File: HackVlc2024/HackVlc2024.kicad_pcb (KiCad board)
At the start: 2 copper layers, 75 x 80 mm, 10 parts, among them J1 Entrada Alimentación, J10 LDR, J2 ESP32_IZQ, J3 ESP32_DER, J4 Neopixel, J5 Lamas, J6 Bomba, J7 Suelo, J8 DH11, J9 Bomba

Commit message: Serigrafia
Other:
- board text added: "Bomba"
- board text added: "DH11"
- board text added: "Entrada Alimentación"
- board text added: "LDR"
- board text added: "Lamas"
- board text added: "Neopixel"
- board text added: "Nivel Tanque"
- board text added: "Suelo"
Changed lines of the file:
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@@
 		(tags "connector JST XH vertical")
 		(property "Reference" "J10"
-			(at 2.5 -3.55 180)
+			(at -6.524 3.344 180)
 			(layer "F.SilkS")
 			(effects
@@
 		(tags "connector JST XH vertical")
 		(property "Reference" "J6"
-			(at 2.5 -3.55 180)
+			(at -6.016 3.344 180)
 			(layer "F.SilkS")
 			(effects
@@
 		(tags "connector JST XH vertical")
 		(property "Reference" "J7"
-			(at 2.5 -3.55 180)
+			(at -6.016 3.344 180)
 			(layer "F.SilkS")
 			(effects
@@
 		(tags "connector JST XH vertical")
 		(property "Reference" "J9"
-			(at 3.75 -3.55 180)
+			(at -6.016 3.81 180)
 			(layer "F.SilkS")
 			(effects
@@
 		(tags "connector JST XH vertical")
 		(property "Reference" "J4"
-			(at 2.5 -3.55 180)
+			(at -6.016 3.344 180)
 			(layer "F.SilkS")
 			(effects
@@
 		(tags "connector JST XH vertical")
 		(property "Reference" "J5"
-			(at 2.5 -3.55 180)
+			(at -6.016 3.344 180)
 			(layer "F.SilkS")
 			(effects
@@
 		(tags "connector JST XH vertical")
 		(property "Reference" "J8"
-			(at 2.5 -3.55 180)
+			(at -6.016 3.344 180)
 			(layer "F.SilkS")
 			(effects
@@
 		(layer "Edge.Cuts")
 	)
+	(gr_text "Suelo"
+		(at 137.668 72.5035 0)
+		(layer "F.SilkS")
+		(effects
+			(font
+				(size 1.5 1.5)
+				(thickness 0.2)
+			)
+			(justify left bottom)
+		)
+	)
+	(gr_text "Bomba"
+		(at 137.668 64.3825 0)
+		(layer "F.SilkS")
+		(effects
+			(font
+				(size 1.5 1.5)
+				(thickness 0.2)
+			)
+			(justify left bottom)
+		)
+	)
+	(gr_text "Nivel\nTanque"
+		(at 137.668 98.073958 0)
+		(layer "F.SilkS")
+		(effects
+			(font
+				(size 1.5 1.5)
+				(thickness 0.2)
+			)
+			(justify left bottom)
+		)
+	)
+	(gr_text "Lamas"
+		(at 137.668 56.2615 0)
+		(layer "F.SilkS")
+		(effects
+			(font
+				(size 1.5 1.5)
+				(thickness 0.2)
+			)
+			(justify left bottom)
+		)
+	)
+	(gr_text "Neopixel"
+		(at 137.668 48.1405 0)
+		(layer "F.SilkS")
+		(effects
+			(font
+				(size 1.5 1.5)
+				(thickness 0.2)
+			)
+			(justify left bottom)
+		)
+	)
+	(gr_text "Entrada Alimentación"
+		(at 90.678 43.942 0)
+		(layer "F.SilkS")
+		(effects
+			(font
+				(size 1.5 1.5)
+				(thickness 0.2)
+				(bold yes)
+			)
+			(justify left bottom)
+		)
+	)
+	(gr_text "LDR"
+		(at 137.668 88.7455 0)
+		(layer "F.SilkS")
+		(effects
+			(font
+				(size 1.5 1.5)
+				(thickness 0.2)
+			)
+			(justify left bottom)
+		)
+	)
+	(gr_text "DH11"
+		(at 137.668 80.6245 0)
+		(layer "F.SilkS")
+		(effects
+			(font
+				(size 1.5 1.5)
+				(thickness 0.2)
+			)
+			(justify left bottom)
+		)
+	)
+	(segment
+		(start 130.81 42.418)
+		(end 132.668 44.276)
+		(width 1.5)
+		(layer "B.Cu")
+		(net 1)
+	)
 	(segment
 		(start 100.584 55.626)
@@
 	)
 	(segment
+		(start 115.824 46.228)
+		(end 119.634 42.418)
+		(width 1.5)
+		(layer "B.Cu")
+		(net 1)
+	)
+	(segment
 		(start 132.668 88.399)
 		(end 132.668 96.52)
@@
 	)
 	(segment
-		(start 115.824 46.228)
-		(end 120.142 41.91)
+		(start 119.634 42.418)
+		(end 130.81 42.418)
 		(width 1.5)
 		(layer "B.Cu")
@@
 	)
 	(segment
-		(start 120.142 41.91)
-		(end 130.302 41.91)
-		(width 1.5)
-		(layer "B.Cu")
-		(net 1)
-	)
-	(segment
 		(start 132.668 47.794)
 		(end 132.668 55.915)
@@
 	)
 	(segment
-		(start 132.668 64.036)
-		(end 132.668 72.157)
+		(start 115.824 55.626)
+		(end 115.824 46.228)
 		(width 1.5)
 		(layer "B.Cu")
@@
 	)
 	(segment
-		(start 115.824 55.626)
-		(end 115.824 46.228)
+		(start 132.668 64.036)
+		(end 132.668 72.157)
 		(width 1.5)
 		(layer "B.Cu")
@@
 	)
 	(segment
-		(start 130.302 41.91)
-		(end 132.668 44.276)
+		(start 132.668 80.278)
+		(end 132.668 88.399)
 		(width 1.5)
 		(layer "B.Cu")
@@
 	)
 	(segment
-		(start 132.668 80.278)
-		(end 132.668 88.399)
-		(width 1.5)
-		(layer "B.Cu")
-		(net 1)
-	)
-	(segment
 		(start 97.282 75.946)
 		(end 95.25 75.946)
@@
 	)
 	(segment
-		(start 130.168 57.538)
-		(end 128.778 58.928)
+		(start 128.778 58.928)
+		(end 127.508 58.928)
 		(width 0.2)
 		(layer "F.Cu")
@@
 	)
 	(segment
-		(start 128.778 58.928)
-		(end 126.492 58.928)
+		(start 127.508 58.928)
+		(end 118.11 68.326)
 		(width 0.2)
 		(layer "F.Cu")
@@
 	)
 	(segment
-		(start 126.492 58.928)
-		(end 117.094 68.326)
+		(start 130.168 55.915)
+		(end 130.168 57.538)
 		(width 0.2)
 		(layer "F.Cu")
@@
 	)
 	(segment
-		(start 130.168 55.915)
-		(end 130.168 57.538)
+		(start 130.168 57.538)
+		(end 128.778 58.928)
 		(width 0.2)
 		(layer "F.Cu")
@@
 	)
 	(segment
-		(start 117.094 68.326)
+		(start 118.11 68.326)
 		(end 115.824 68.326)
 		(width 0.2)

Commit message: Versión final de hoy por la mañana
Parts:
- J1: footprint Connector_PinHeader_2.54mm:PinHeader_1x02_P2.54mm_Vertical -> TerminalBlock_Phoenix:TerminalBlock_Phoenix_MKDS-1,5-2_1x02_P5.00mm_Horizontal
- J2, J3: footprint Connector_PinHeader_2.54mm:PinHeader_1x15_P2.54mm_Vertical -> Connector_PinSocket_2.54mm:PinSocket_1x15_P2.54mm_Vertical
- moved J1 9.36 mm to (106.7, 48.2), turned to 180 degrees
- moved J2 3.05 mm to (95.2, 58.7)
- moved J3 3.05 mm to (115.8, 58.7)
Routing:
- net /D27: track 20.4 -> 22.4 mm
- net /D26: track 18.3 -> 20.1 mm
- net +5V: track 107.8 -> 106.2 mm
- net /D33: track 16.7 -> 18.0 mm
- net /D4: track 40.9 -> 39.7 mm
- net /D5: track 51.2 -> 50.0 mm
- net /D25: track 21.8 -> 20.8 mm
- net /D14: track 27.2 -> 28.0 mm
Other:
- board size 75 x 80 mm -> 60 x 65 mm

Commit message: Pin luz a 32
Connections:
- J10 pad 2: /D25 -> /D32
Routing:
- net /D25: track 20.8 -> 0.00 mm
- net /D32: track 0.00 -> 18.6 mm
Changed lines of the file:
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@@
 			(layers "*.Cu" "*.Mask")
 			(remove_unused_layers no)
-			(net 20 "/D25")
+			(net 26 "/D32")
 			(pinfunction "Pin_2")
 			(pintype "passive")
@@
 	)
 	(segment
-		(start 130.168 86.226)
-		(end 120.396 76.454)
-		(width 0.2)
-		(layer "B.Cu")
-		(net 20)
-	)
-	(segment
-		(start 120.396 76.454)
-		(end 116.332 76.454)
-		(width 0.2)
-		(layer "B.Cu")
-		(net 20)
-	)
-	(segment
-		(start 130.168 88.399)
-		(end 130.168 86.226)
-		(width 0.2)
-		(layer "B.Cu")
-		(net 20)
-	)
-	(segment
-		(start 116.332 76.454)
-		(end 115.824 75.946)
-		(width 0.2)
-		(layer "B.Cu")
-		(net 20)
-	)
-	(segment
 		(start 115.824 71.374)
 		(end 117.602 71.374)
@@
 		(net 24)
 	)
+	(segment
+		(start 130.168 85.972)
+		(end 125.73 81.534)
+		(width 0.2)
+		(layer "F.Cu")
+		(net 26)
+	)
+	(segment
+		(start 130.168 88.399)
+		(end 130.168 85.972)
+		(width 0.2)
+		(layer "F.Cu")
+		(net 26)
+	)
+	(segment
+		(start 125.73 81.534)
+		(end 115.824 81.534)
+		(width 0.2)
+		(layer "F.Cu")
+		(net 26)
+	)
 	(zone

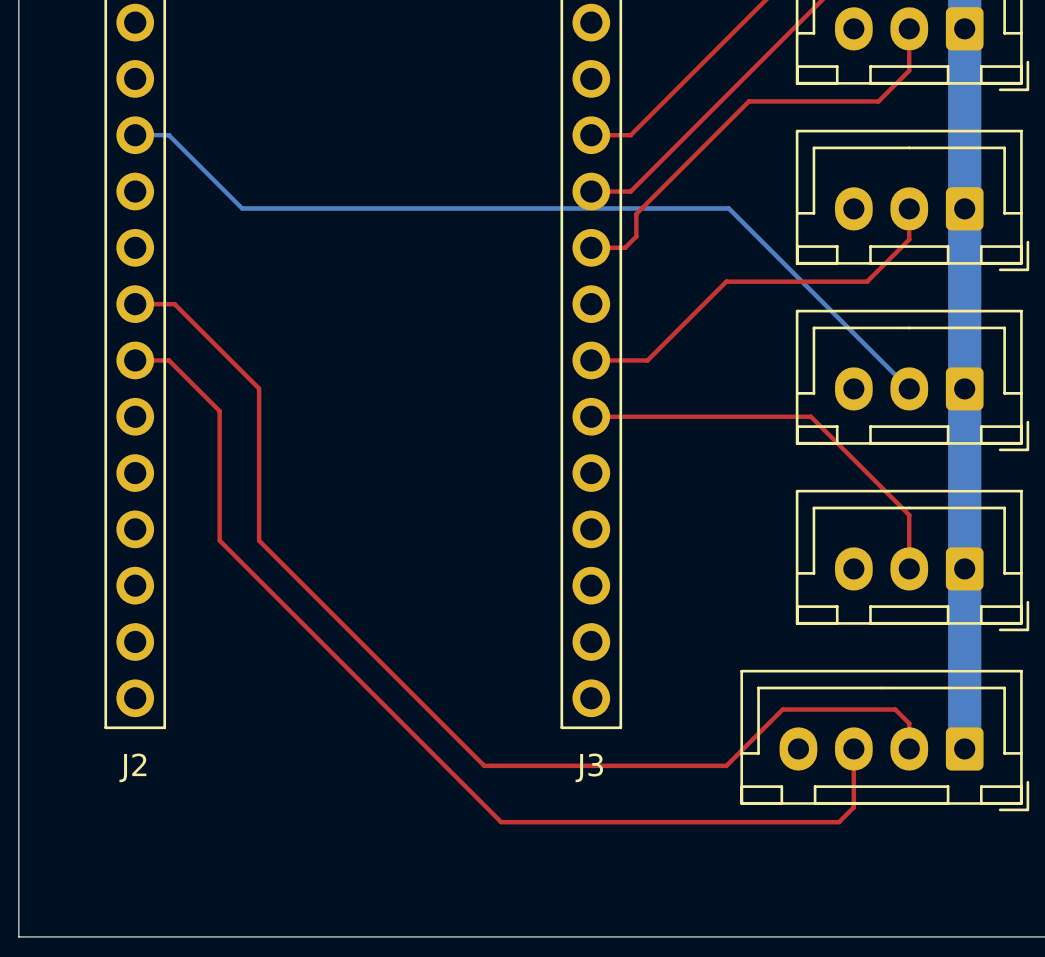
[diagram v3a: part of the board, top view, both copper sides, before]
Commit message: Pin 4 cambiado a 34
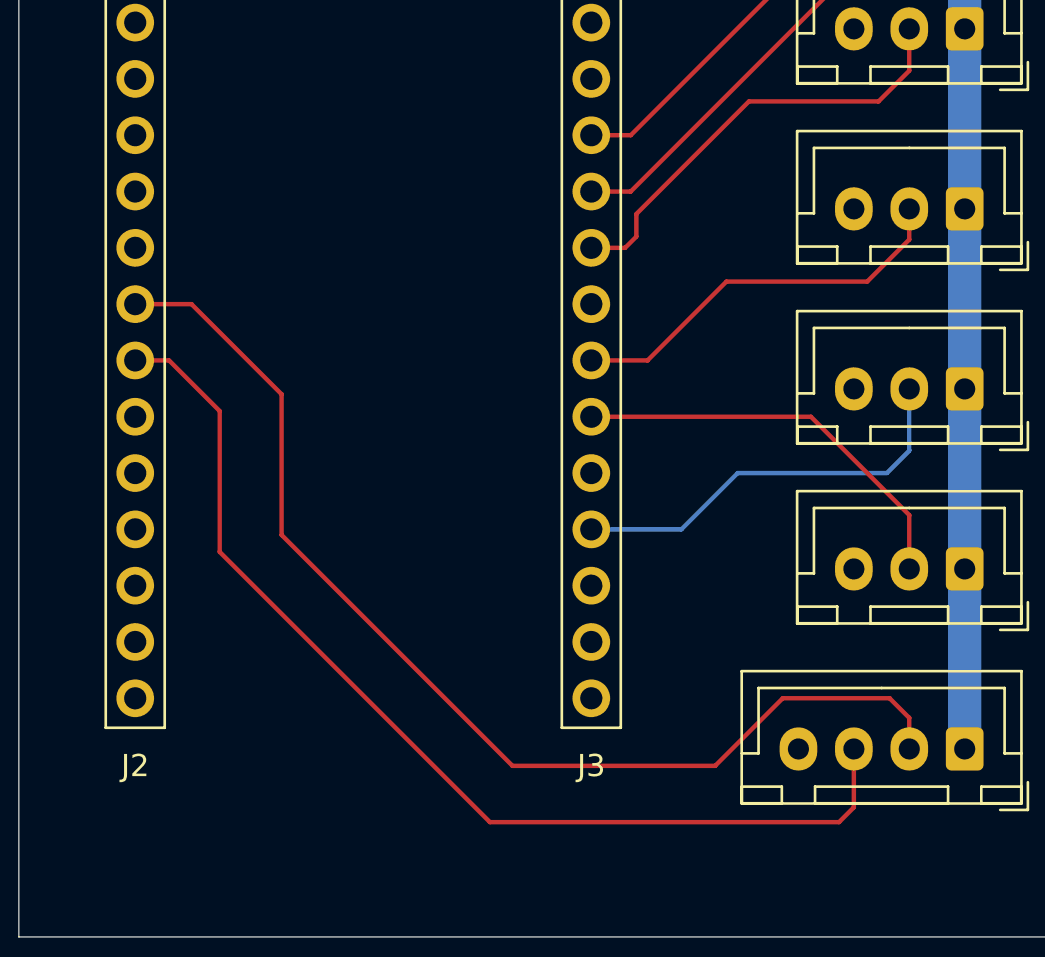
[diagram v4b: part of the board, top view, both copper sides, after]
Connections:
- J8 pad 2: /D4 -> /D34
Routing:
- net /D4: track 39.7 -> 0.00 mm
- net /D34: track 0.00 -> 18.6 mm
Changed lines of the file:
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@@
 			(layers "*.Cu" "*.Mask")
 			(remove_unused_layers no)
-			(net 11 "/D4")
+			(net 21 "/D34")
 			(pinfunction "Pin_2")
 			(pintype "passive")
@@
 	)
 	(segment
-		(start 99.06 81.28)
-		(end 99.06 87.122)
-		(width 0.2)
-		(layer "F.Cu")
-		(net 3)
-	)
-	(segment
 		(start 127.668 99.154)
 		(end 127.668 96.52)
@@
 	)
 	(segment
+		(start 99.06 87.63)
+		(end 111.252 99.822)
+		(width 0.2)
+		(layer "F.Cu")
+		(net 3)
+	)
+	(segment
+		(start 99.06 81.28)
+		(end 99.06 87.63)
+		(width 0.2)
+		(layer "F.Cu")
+		(net 3)
+	)
+	(segment
+		(start 95.25 78.994)
+		(end 96.774 78.994)
+		(width 0.2)
+		(layer "F.Cu")
+		(net 3)
+	)
+	(segment
+		(start 111.252 99.822)
+		(end 127 99.822)
+		(width 0.2)
+		(layer "F.Cu")
+		(net 3)
+	)
+	(segment
 		(start 127 99.822)
 		(end 127.668 99.154)
@@
 	)
 	(segment
-		(start 111.76 99.822)
-		(end 127 99.822)
-		(width 0.2)
-		(layer "F.Cu")
-		(net 3)
-	)
-	(segment
 		(start 96.774 78.994)
 		(end 99.06 81.28)
@@
 	)
 	(segment
-		(start 95.25 78.994)
-		(end 96.774 78.994)
-		(width 0.2)
-		(layer "F.Cu")
-		(net 3)
-	)
-	(segment
-		(start 99.06 87.122)
-		(end 111.76 99.822)
-		(width 0.2)
-		(layer "F.Cu")
-		(net 3)
-	)
-	(segment
-		(start 100.838 87.122)
-		(end 100.838 80.264)
+		(start 130.168 96.52)
+		(end 130.168 95.116)
 		(width 0.2)
 		(layer "F.Cu")
@@
 	)
 	(segment
-		(start 97.028 76.454)
+		(start 121.412 97.282)
+		(end 112.268 97.282)
+		(width 0.2)
+		(layer "F.Cu")
+		(net 9)
+	)
+	(segment
+		(start 101.854 80.518)
+		(end 97.79 76.454)
+		(width 0.2)
+		(layer "F.Cu")
+		(net 9)
+	)
+	(segment
+		(start 112.268 97.282)
+		(end 101.854 86.868)
+		(width 0.2)
+		(layer "F.Cu")
+		(net 9)
+	)
+	(segment
+		(start 101.854 86.868)
+		(end 101.854 80.518)
+		(width 0.2)
+		(layer "F.Cu")
+		(net 9)
+	)
+	(segment
+		(start 124.46 94.234)
+		(end 121.412 97.282)
+		(width 0.2)
+		(layer "F.Cu")
+		(net 9)
+	)
+	(segment
+		(start 130.168 95.116)
+		(end 129.286 94.234)
+		(width 0.2)
+		(layer "F.Cu")
+		(net 9)
+	)
+	(segment
+		(start 129.286 94.234)
+		(end 124.46 94.234)
+		(width 0.2)
+		(layer "F.Cu")
+		(net 9)
+	)
+	(segment
+		(start 97.79 76.454)
 		(end 95.25 76.454)
 		(width 0.2)
 		(layer "F.Cu")
 		(net 9)
-	)
-	(segment
-		(start 130.168 96.52)
-		(end 130.168 95.37)
-		(width 0.2)
-		(layer "F.Cu")
-		(net 9)
-	)
-	(segment
-		(start 121.92 97.282)
-		(end 110.998 97.282)
-		(width 0.2)
-		(layer "F.Cu")
-		(net 9)
-	)
-	(segment
-		(start 110.998 97.282)
-		(end 100.838 87.122)
-		(width 0.2)
-		(layer "F.Cu")
-		(net 9)
-	)
-	(segment
-		(start 129.54 94.742)
-		(end 124.46 94.742)
-		(width 0.2)
-		(layer "F.Cu")
-		(net 9)
-	)
-	(segment
-		(start 130.168 95.37)
-		(end 129.54 94.742)
-		(width 0.2)
-		(layer "F.Cu")
-		(net 9)
-	)
-	(segment
-		(start 100.838 80.264)
-		(end 97.028 76.454)
-		(width 0.2)
-		(layer "F.Cu")
-		(net 9)
-	)
-	(segment
-		(start 124.46 94.742)
-		(end 121.92 97.282)
-		(width 0.2)
-		(layer "F.Cu")
-		(net 9)
-	)
-	(segment
-		(start 96.774 68.834)
-		(end 95.25 68.834)
-		(width 0.2)
-		(layer "B.Cu")
-		(net 11)
-	)
-	(segment
-		(start 100.076 72.136)
-		(end 96.774 68.834)
-		(width 0.2)
-		(layer "B.Cu")
-		(net 11)
-	)
-	(segment
-		(start 130.168 80.278)
-		(end 122.026 72.136)
-		(width 0.2)
-		(layer "B.Cu")
-		(net 11)
-	)
-	(segment
-		(start 122.026 72.136)
-		(end 100.076 72.136)
-		(width 0.2)
-		(layer "B.Cu")
-		(net 11)
 	)
 	(segment
@@
 	)
 	(segment
+		(start 119.888 86.614)
+		(end 115.824 86.614)
+		(width 0.2)
+		(layer "B.Cu")
+		(net 21)
+	)
+	(segment
+		(start 130.168 83.065)
+		(end 129.159 84.074)
+		(width 0.2)
+		(layer "B.Cu")
+		(net 21)
+	)
+	(segment
+		(start 129.159 84.074)
+		(end 122.428 84.074)
+		(width 0.2)
+		(layer "B.Cu")
+		(net 21)
+	)
+	(segment
+		(start 122.428 84.074)
+		(end 119.888 86.614)
+		(width 0.2)
+		(layer "B.Cu")
+		(net 21)
+	)
+	(segment
+		(start 130.168 80.278)
+		(end 130.168 83.065)
+		(width 0.2)
+		(layer "B.Cu")
+		(net 21)
+	)
+	(segment

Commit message: D34 vuelve a ser D4
Por el DH11
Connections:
- J8 pad 2: /D34 -> /D4
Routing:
- net /D4: track 0.00 -> 40.8 mm
- net /D34: track 18.6 -> 0.00 mm
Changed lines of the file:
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@@
 			(layers "*.Cu" "*.Mask")
 			(remove_unused_layers no)
-			(net 21 "/D34")
+			(net 11 "/D4")
 			(pinfunction "Pin_2")
 			(pintype "passive")
@@
 	)
 	(segment
+		(start 130.168 78.352)
+		(end 121.8 69.984)
+		(width 0.2)
+		(layer "B.Cu")
+		(net 11)
+	)
+	(segment
+		(start 102.87 68.834)
+		(end 95.25 68.834)
+		(width 0.2)
+		(layer "B.Cu")
+		(net 11)
+	)
+	(segment
+		(start 121.8 69.984)
+		(end 104.02 69.984)
+		(width 0.2)
+		(layer "B.Cu")
+		(net 11)
+	)
+	(segment
+		(start 104.02 69.984)
+		(end 102.87 68.834)
+		(width 0.2)
+		(layer "B.Cu")
+		(net 11)
+	)
+	(segment
+		(start 130.168 80.278)
+		(end 130.168 78.352)
+		(width 0.2)
+		(layer "B.Cu")
+		(net 11)
+	)
+	(segment
 		(start 125.73 60.706)
 		(end 125.73 54.356)
@@
 	)
 	(segment
-		(start 119.888 86.614)
-		(end 115.824 86.614)
-		(width 0.2)
-		(layer "B.Cu")
-		(net 21)
-	)
-	(segment
-		(start 130.168 83.065)
-		(end 129.159 84.074)
-		(width 0.2)
-		(layer "B.Cu")
-		(net 21)
-	)
-	(segment
-		(start 129.159 84.074)
-		(end 122.428 84.074)
-		(width 0.2)
-		(layer "B.Cu")
-		(net 21)
-	)
-	(segment
-		(start 122.428 84.074)
-		(end 119.888 86.614)
-		(width 0.2)
-		(layer "B.Cu")
-		(net 21)
-	)
-	(segment
-		(start 130.168 80.278)
-		(end 130.168 83.065)
-		(width 0.2)
-		(layer "B.Cu")
-		(net 21)
-	)
-	(segment
